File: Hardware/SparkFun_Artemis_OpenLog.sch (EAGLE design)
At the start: 87 parts, among them J14 CORTEX_JTAG, J17 MICRO-SD, Q1 20V/0.2A/8MHz/1.2Ω/1Vth, Q10 20V/0.2A/8MHz/1.2Ω/1Vth, Q2 20V/4.2A/52mΩ/1.4W, Q3 20V/0.2A/8MHz/1.2Ω/1Vth, Q4 20V/4.2A/52mΩ/1.4W, Q7 20V/0.2A/8MHz/1.2Ω/1Vth, Q9 20V/0.2A/8MHz/1.2Ω/1Vth, U1 3.0V Supervisor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

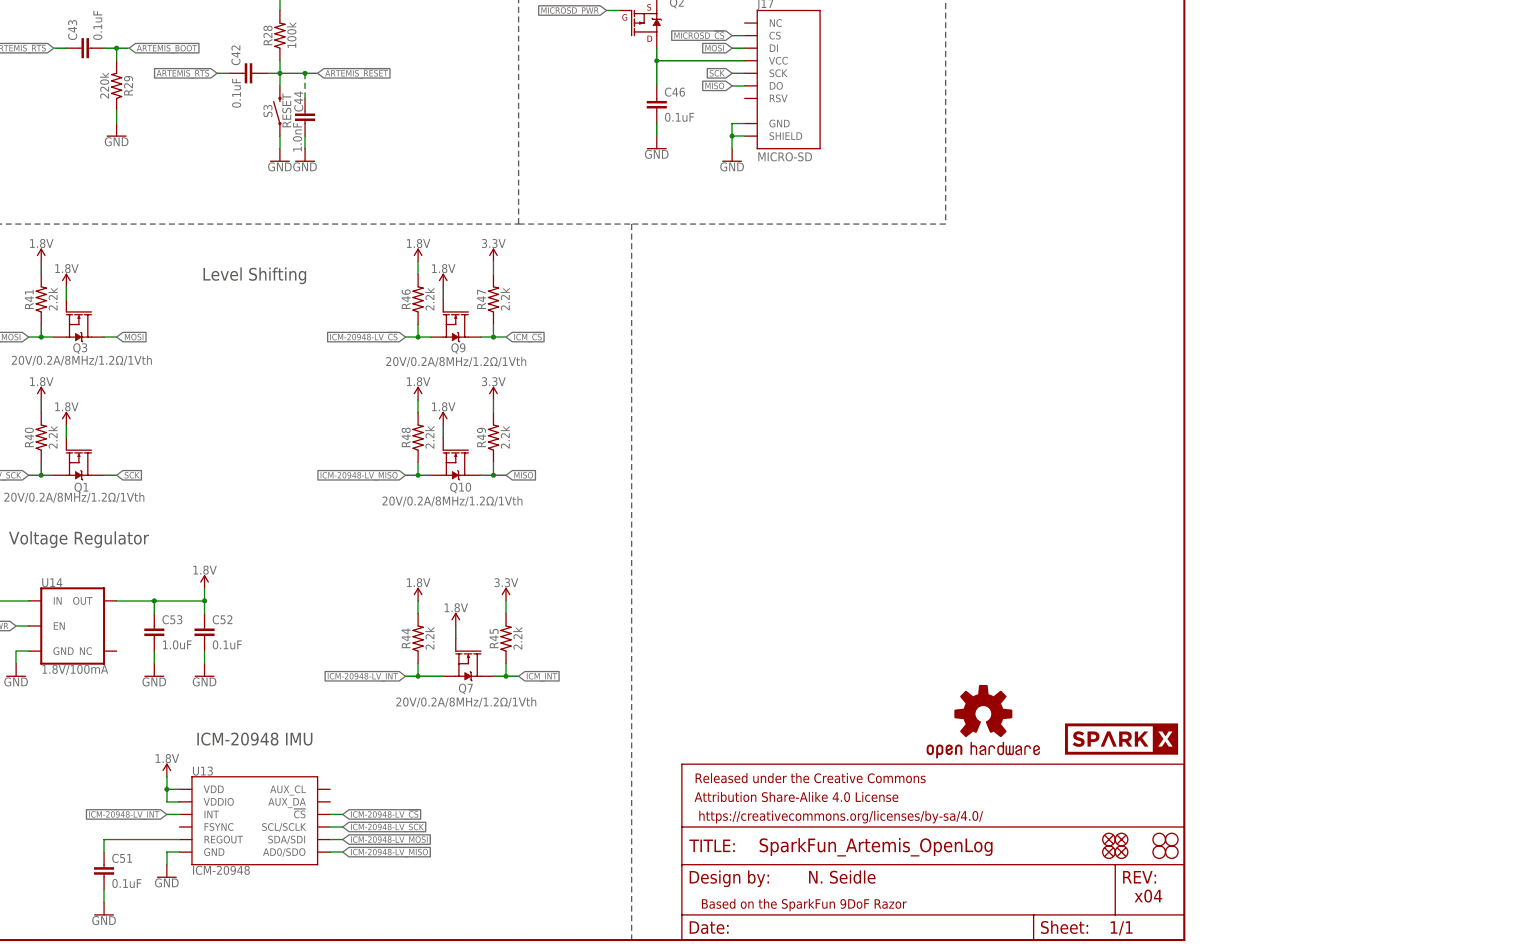
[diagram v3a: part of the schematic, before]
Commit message: First steps towards multi-device detection
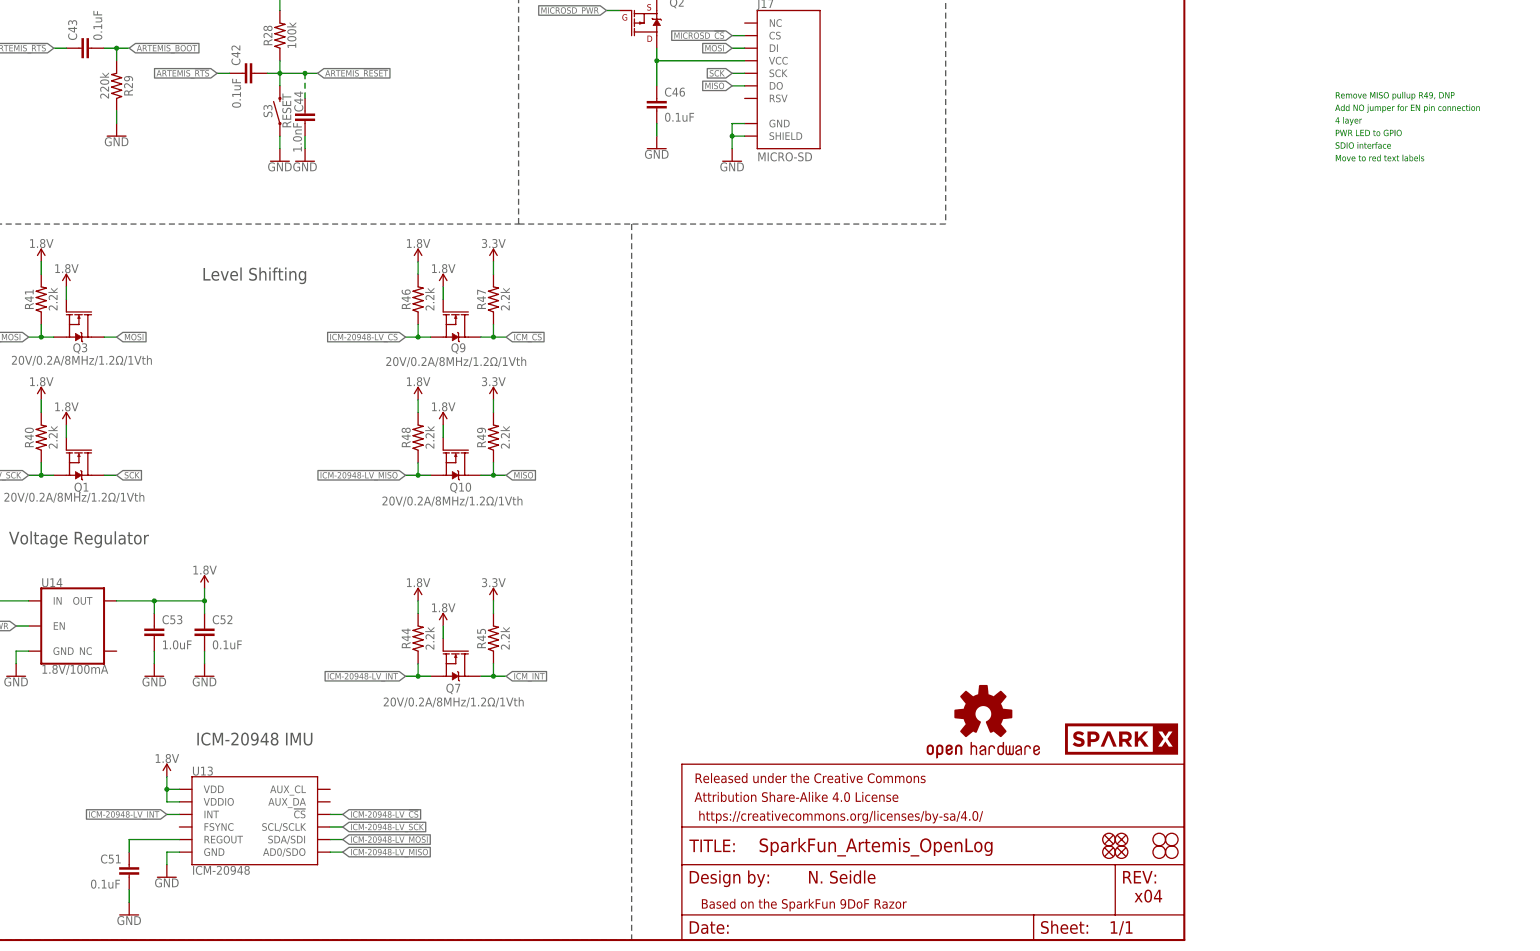
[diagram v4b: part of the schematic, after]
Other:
- note added: "4 layer"
- note added: "Add NO jumper for EN pin connection"
- note added: "Move to red text labels"
- note added: "PWR LED to GPIO"
- note added: "Remove MISO pullup R49, DNP"
- note added: "SDIO interface"
- moved on the sheet: C51, Q7, R45
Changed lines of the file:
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@@
 <wire x1="383.54" y1="210.82" x2="383.54" y2="144.78" width="0.2032" layer="97" style="longdash"/>
 <wire x1="383.54" y1="144.78" x2="320.04" y2="144.78" width="0.2032" layer="97" style="longdash"/>
+<text x="462.28" y="170.18" size="1.27" layer="91">Remove MISO pullup R49, DNP</text>
+<text x="462.28" y="167.64" size="1.27" layer="91">Add NO jumper for EN pin connection</text>
+<text x="462.28" y="165.1" size="1.27" layer="91">4 layer</text>
+<text x="462.28" y="160.02" size="1.27" layer="91">SDIO interface</text>
+<text x="462.28" y="162.56" size="1.27" layer="91">PWR LED to GPIO</text>
+<text x="462.28" y="157.48" size="1.27" layer="91">Move to red text labels</text>
 </plain>
 <instances>
@@
 <attribute name="VALUE" x="231.14" y="14.986" size="1.778" layer="96" font="vector" align="top-left"/>
 </instance>
-<instance part="C51" gate="G$1" x="213.36" y="12.7" smashed="yes">
-<attribute name="NAME" x="214.884" y="15.621" size="1.778" layer="95" font="vector"/>
-<attribute name="VALUE" x="214.884" y="10.541" size="1.778" layer="96" font="vector"/>
+<instance part="C51" gate="G$1" x="218.44" y="12.7" smashed="yes">
+<attribute name="NAME" x="212.598" y="15.494" size="1.778" layer="95" font="vector"/>
+<attribute name="VALUE" x="210.566" y="10.414" size="1.778" layer="96" font="vector"/>
 </instance>
 <instance part="C52" gate="G$1" x="233.68" y="60.96" smashed="yes">
@@
 <attribute name="VALUE" x="226.06" y="12.446" size="1.778" layer="96" align="top-center"/>
 </instance>
-<instance part="GND81" gate="1" x="213.36" y="5.08" smashed="yes">
-<attribute name="VALUE" x="213.36" y="4.826" size="1.778" layer="96" align="top-center"/>
+<instance part="GND81" gate="1" x="218.44" y="5.08" smashed="yes">
+<attribute name="VALUE" x="218.44" y="4.826" size="1.778" layer="96" align="top-center"/>
 </instance>
 <instance part="GND82" gate="1" x="233.68" y="53.34" smashed="yes">
@@
 <attribute name="VALUE" x="200.66" y="139.954" size="1.778" layer="96" align="bottom-center"/>
 </instance>
-<instance part="Q7" gate="NMOS" x="287.02" y="55.88" smashed="yes" rot="R270">
-<attribute name="NAME" x="284.988" y="50.038" size="1.778" layer="95" font="vector"/>
-<attribute name="VALUE" x="272.288" y="47.244" size="1.778" layer="96" font="vector"/>
+<instance part="Q7" gate="NMOS" x="284.48" y="55.88" smashed="yes" rot="R270">
+<attribute name="NAME" x="282.448" y="50.038" size="1.778" layer="95" font="vector"/>
+<attribute name="VALUE" x="269.748" y="47.244" size="1.778" layer="96" font="vector"/>
 </instance>
 <instance part="R44" gate="G$1" x="276.86" y="60.96" smashed="yes" rot="R90">
@@
 <attribute name="VALUE" x="278.384" y="60.96" size="1.778" layer="96" font="vector" rot="R90" align="top-center"/>
 </instance>
-<instance part="R45" gate="G$1" x="294.64" y="60.96" smashed="yes" rot="R90">
-<attribute name="NAME" x="293.116" y="60.96" size="1.778" layer="95" font="vector" rot="R90" align="bottom-center"/>
-<attribute name="VALUE" x="296.164" y="60.96" size="1.778" layer="96" font="vector" rot="R90" align="top-center"/>
+<instance part="R45" gate="G$1" x="292.1" y="60.96" smashed="yes" rot="R90">
+<attribute name="NAME" x="290.576" y="60.96" size="1.778" layer="95" font="vector" rot="R90" align="bottom-center"/>
+<attribute name="VALUE" x="293.624" y="60.96" size="1.778" layer="96" font="vector" rot="R90" align="top-center"/>
 </instance>
 <instance part="SUPPLY72" gate="G$1" x="276.86" y="68.58" smashed="yes">
@@
 <attribute name="VALUE" x="177.8" y="73.914" size="1.778" layer="96" align="bottom-center"/>
 </instance>
-<instance part="SUPPLY75" gate="G$1" x="294.64" y="68.58" smashed="yes">
-<attribute name="VALUE" x="294.64" y="71.374" size="1.778" layer="96" align="bottom-center"/>
+<instance part="SUPPLY75" gate="G$1" x="292.1" y="68.58" smashed="yes">
+<attribute name="VALUE" x="292.1" y="71.374" size="1.778" layer="96" align="bottom-center"/>
 </instance>
 <instance part="GND85" gate="1" x="195.58" y="53.34" smashed="yes">
@@
 <attribute name="VALUE" x="205.74" y="134.874" size="1.778" layer="96" align="bottom-center"/>
 </instance>
-<instance part="SUPPLY79" gate="G$1" x="284.48" y="63.5" smashed="yes">
-<attribute name="VALUE" x="284.48" y="66.294" size="1.778" layer="96" align="bottom-center"/>
+<instance part="SUPPLY79" gate="G$1" x="281.94" y="63.5" smashed="yes">
+<attribute name="VALUE" x="281.94" y="66.294" size="1.778" layer="96" align="bottom-center"/>
 </instance>
 <instance part="SUPPLY80" gate="G$1" x="226.06" y="33.02" smashed="yes">
@@
 <pinref part="C51" gate="G$1" pin="2"/>
 <pinref part="GND81" gate="1" pin="GND"/>
-<wire x1="213.36" y1="10.16" x2="213.36" y2="7.62" width="0.1524" layer="91"/>
+<wire x1="218.44" y1="10.16" x2="218.44" y2="7.62" width="0.1524" layer="91"/>
 </segment>
 <segment>
@@
 <segment>
 <pinref part="R45" gate="G$1" pin="2"/>
-<wire x1="294.64" y1="66.04" x2="294.64" y2="68.58" width="0.1524" layer="91"/>
+<wire x1="292.1" y1="66.04" x2="292.1" y2="68.58" width="0.1524" layer="91"/>
 <pinref part="SUPPLY75" gate="G$1" pin="3.3V"/>
 </segment>
@@
 <segment>
 <pinref part="U13" gate="G$1" pin="REGOUT"/>
-<wire x1="228.6" y1="20.32" x2="213.36" y2="20.32" width="0.1524" layer="91"/>
+<wire x1="228.6" y1="20.32" x2="218.44" y2="20.32" width="0.1524" layer="91"/>
 <pinref part="C51" gate="G$1" pin="1"/>
-<wire x1="213.36" y1="20.32" x2="213.36" y2="17.78" width="0.1524" layer="91"/>
+<wire x1="218.44" y1="20.32" x2="218.44" y2="17.78" width="0.1524" layer="91"/>
 </segment>
 </net>
@@
 <segment>
 <pinref part="Q7" gate="NMOS" pin="S"/>
-<wire x1="276.86" y1="53.34" x2="281.94" y2="53.34" width="0.1524" layer="91"/>
+<wire x1="276.86" y1="53.34" x2="279.4" y2="53.34" width="0.1524" layer="91"/>
 <wire x1="274.32" y1="53.34" x2="276.86" y2="53.34" width="0.1524" layer="91"/>
 <pinref part="R44" gate="G$1" pin="1"/>
@@
 </segment>
 <segment>
-<wire x1="284.48" y1="63.5" x2="284.48" y2="60.96" width="0.1524" layer="91"/>
+<wire x1="281.94" y1="63.5" x2="281.94" y2="60.96" width="0.1524" layer="91"/>
 <pinref part="SUPPLY79" gate="G$1" pin="1.8V"/>
 <pinref part="Q7" gate="NMOS" pin="G"/>
@@
 <segment>
 <pinref part="R45" gate="G$1" pin="1"/>
-<wire x1="294.64" y1="55.88" x2="294.64" y2="53.34" width="0.1524" layer="91"/>
+<wire x1="292.1" y1="55.88" x2="292.1" y2="53.34" width="0.1524" layer="91"/>
 <pinref part="Q7" gate="NMOS" pin="D"/>
+<wire x1="289.56" y1="53.34" x2="292.1" y2="53.34" width="0.1524" layer="91"/>
 <wire x1="292.1" y1="53.34" x2="294.64" y2="53.34" width="0.1524" layer="91"/>
-<wire x1="294.64" y1="53.34" x2="297.18" y2="53.34" width="0.1524" layer="91"/>
-<junction x="294.64" y="53.34"/>
-<label x="297.18" y="53.34" size="1.27" layer="95" xref="yes"/>
-</segment>
-<segment>
+<junction x="292.1" y="53.34"/>
+<label x="294.64" y="53.34" size="1.27" layer="95" xref="yes"/>
+</segment>
+<segment>
